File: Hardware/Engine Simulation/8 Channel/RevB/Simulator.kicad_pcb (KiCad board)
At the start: 2 copper layers, 100 x 80 mm, 69 parts, among them IC1 EL357NB_TA_-G, IC2 EL357NB_TA_-G, J1 Conn_02x20_Counter_Clockwise, J2 Conn_01x08, J3 Conn_01x08, J4 Conn_01x04, J5 Conn_01x04, J6 Conn_01x04, J7 Conn_01x10, J8 Conn_01x03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

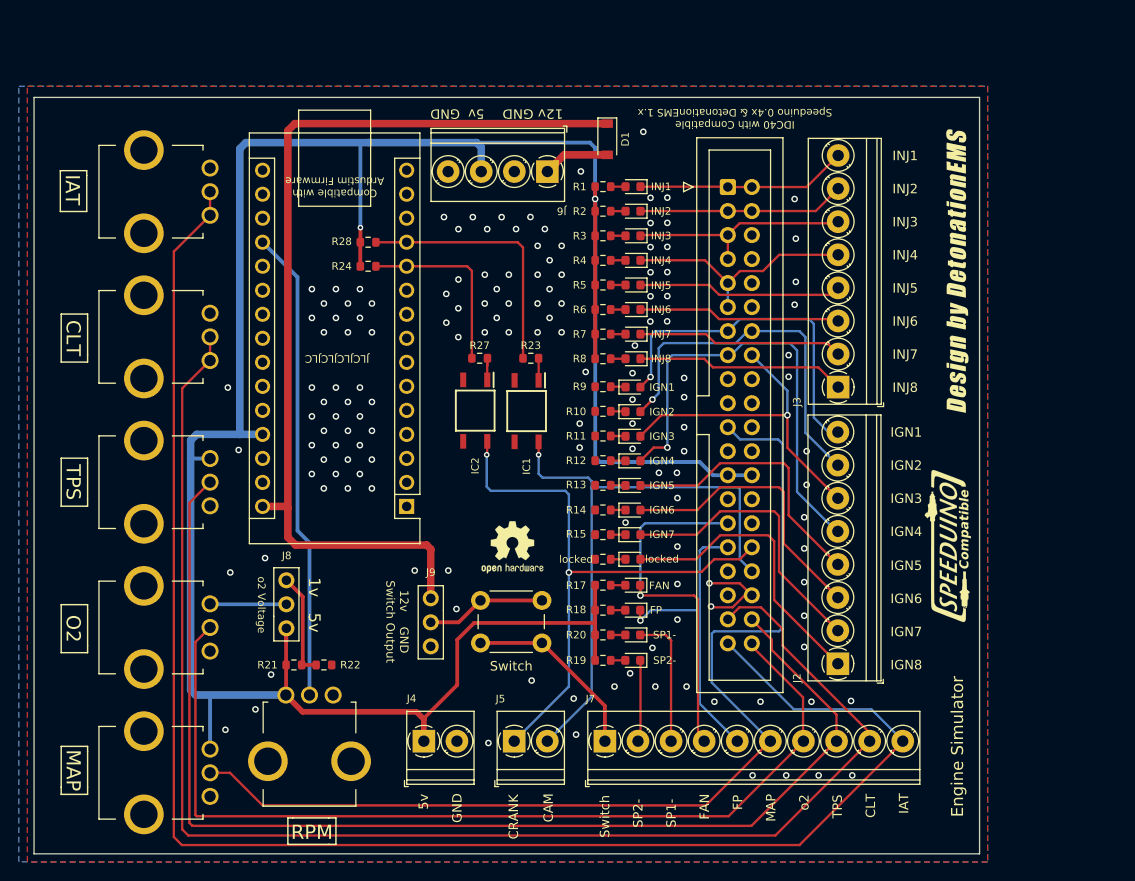
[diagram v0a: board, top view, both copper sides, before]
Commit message: Engine Simulator Upload Revision Correcton
Minor changes were made to RevB and uploaded as RevC by mistake. RevB minor layout changes for ease of use. Protection Zener added. Label correction.
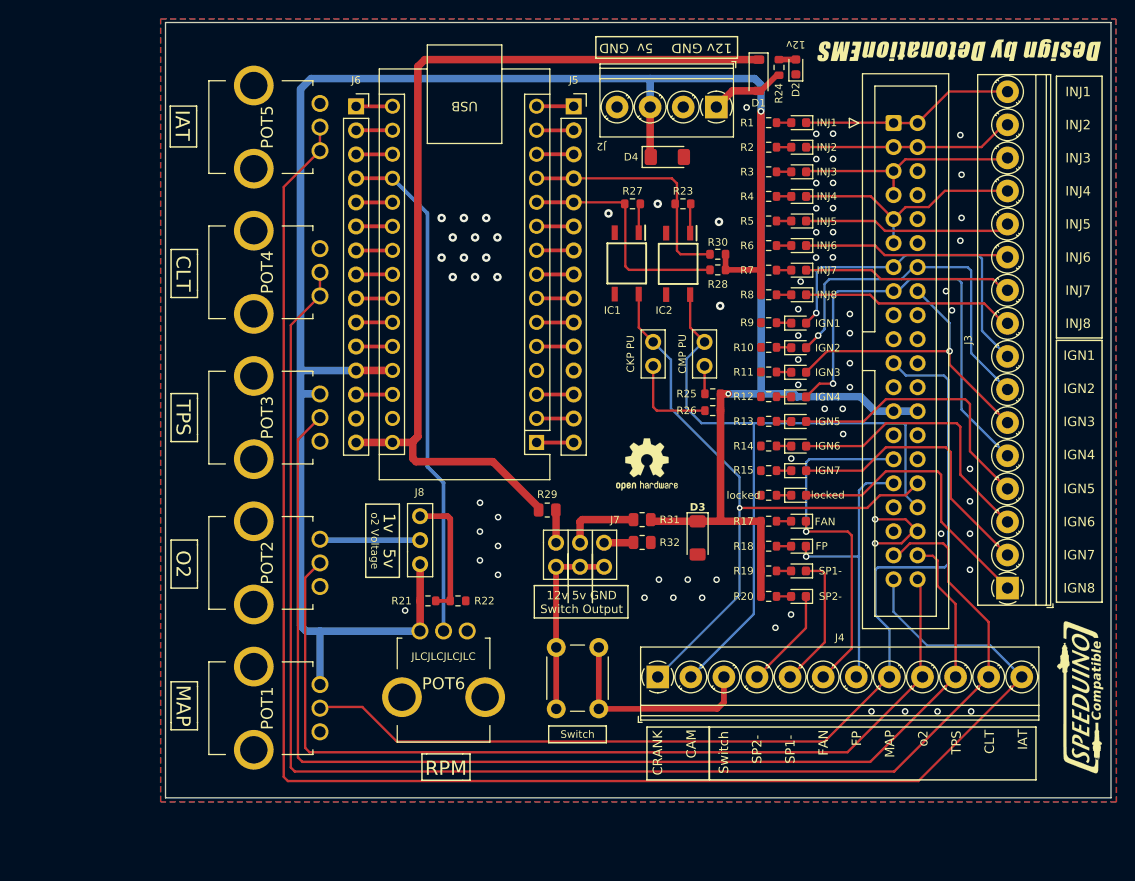
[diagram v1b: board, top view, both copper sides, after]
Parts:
- removed the J3 at (170.0, 96.5)
- removed the J4 at (126.1, 133.9)
- added D2: 12v, LED_SMD:LED_0603_1608Metric, F.Cu at (165.5, 62.6)
- added D3: ZMM5V6, Diode_SMD:D_MiniMELF, F.Cu at (155.1, 112.4)
- added D4: ZMM5V6, Diode_SMD:D_MiniMELF, F.Cu at (151.9, 72.1)
- added J10: CMP PU, Detonation:1x02-Proto, F.Cu at (155.8, 94.2)
- added J6: Conn_01x04, Connector_PinSocket_2.54mm:PinSocket_1x15_P2.54mm_Vertical, F.Cu at (119.0, 66.8)
- added J9: CKP PU, Detonation:1x02-Proto, F.Cu at (150.4, 94.2)
- added R25: 1k, Resistor_SMD:R_0603_1608Metric, F.Cu at (156.7, 97.2)
- added R26: 1k, Resistor_SMD:R_0603_1608Metric, F.Cu at (156.7, 99.0)
- added R29: 0r, Resistor_SMD:R_0805_2012Metric, F.Cu at (139.2, 109.5)
- added R30: 1k, Resistor_SMD:R_0603_1608Metric, F.Cu at (157.2, 82.4)
- added R31: 0r, Resistor_SMD:R_0805_2012Metric, F.Cu at (149.2, 110.5)
- added R32: 0r, Resistor_SMD:R_0805_2012Metric, F.Cu at (149.2, 112.9)
- D1: value SS34 -> B5819W
- J3: renamed from J2; footprint TerminalBlock_Phoenix:TerminalBlock_Phoenix_PT-1,5-8-3.5-H_1x08_P3.50mm_Horizontal -> TerminalBlock_Phoenix:TerminalBlock_Phoenix_PT-1,5-16-3.5-H_1x16_P3.50mm_Horizontal
- J4: renamed from J7; footprint TerminalBlock_Phoenix:TerminalBlock_Phoenix_PT-1,5-10-3.5-H_1x10_P3.50mm_Horizontal -> TerminalBlock_Phoenix:TerminalBlock_Phoenix_PT-1,5-12-3.5-H_1x12_P3.50mm_Horizontal
- J5: footprint TerminalBlock_Phoenix:TerminalBlock_Phoenix_PT-1,5-2-3.5-H_1x02_P3.50mm_Horizontal -> Connector_PinSocket_2.54mm:PinSocket_1x15_P2.54mm_Vertical
- J7: renamed from J9; footprint Detonation:3-PinSwitch -> Detonation:PinSocket 2x03
- POT1, POT2, POT3, POT4, POT5, POT6: footprint MyLibs:RV09AF4020KB10K -> Misc:RV09AF4020KB10K
- R1, R10, R11, R12, R13, R14, R15, R17, R18, R2, R3, R4, R5, R6, R7, R8, R9, locked: value 470 -> 1k
- R19: renamed from R20; value 470 -> 1k
- R20: renamed from R19; value 470 -> 1k
- R21, R23, R27: value 470 -> 470r
- R22: value 100 -> 100r
- R24, R28: value 10k -> 1k
- moved J5 67.4 mm to (142.0, 66.8)
- moved R24 48.3 mm to (163.7, 62.7), turned to 90 degrees
- moved R28 37.1 mm to (157.2, 84.1)
- moved G1 23.4 mm to (182.8, 60.8), turned to 180 degrees
- moved R27 23.0 mm to (148.2, 77.1)
- moved R23 22.9 mm to (153.5, 77.1)
- moved IC2 22.3 mm to (153.0, 83.4)
- moved IC1 22.3 mm to (147.6, 83.4)
- moved G2 21.3 mm to (195.5, 129.3)
- moved J3 19.6 mm to (187.9, 117.7)
- moved J2 19.1 mm to (157.1, 66.9)
- moved J1 18.8 mm to (175.8, 68.5)
- moved LED10 18.8 mm to (165.8, 92.3)
- moved LED14 18.8 mm to (165.8, 102.7)
- moved LED15 18.8 mm to (165.8, 105.3)
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- renumbered IC2 to IC1, IC1 to IC2, J6 to J2, LED20 to LED19, LED19 to LED20
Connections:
- A1 pad 1: unconnected-(A1-Pad1) -> MC-D1
- A1 pad 10: unconnected-(A1-Pad10) -> MC-D7
- A1 pad 13: unconnected-(A1-Pad13) -> MC-D10
- A1 pad 14: unconnected-(A1-Pad14) -> MC-D11
- A1 pad 15: unconnected-(A1-Pad15) -> MC-D12
- A1 pad 16: unconnected-(A1-Pad16) -> MC-D13
- A1 pad 17: unconnected-(A1-Pad17) -> +3.3V
- A1 pad 18: unconnected-(A1-Pad18) -> MC-AREF
- A1 pad 20: unconnected-(A1-Pad20) -> MC-A1
- A1 pad 21: unconnected-(A1-Pad21) -> MC-A2
- A1 pad 22: unconnected-(A1-Pad22) -> MC-A3
- A1 pad 23: unconnected-(A1-Pad23) -> MC-A4
- A1 pad 24: unconnected-(A1-Pad24) -> MC-A5
- A1 pad 25: unconnected-(A1-Pad25) -> MC-A6
- A1 pad 26: unconnected-(A1-Pad26) -> MC-A7
- A1 pad 28: unconnected-(A1-Pad28) -> MC-RESET-28
- A1 pad 3: unconnected-(A1-Pad3) -> MC-RESET-3
- A1 pad 5: unconnected-(A1-Pad5) -> MC-D2
- A1 pad 6: unconnected-(A1-Pad6) -> MC-D3
- A1 pad 7: unconnected-(A1-Pad7) -> MC-D4
- A1 pad 8: unconnected-(A1-Pad8) -> MC-D5
- A1 pad 9: unconnected-(A1-Pad9) -> MC-D6
- D1 pad 2: +BATT -> 12v-Unprotected
- J2 pad 1: +BATT -> 12v-Unprotected
- J4 pad 1: SWITCH -> CRANK-OUT
- J4 pad 10: IAT -> TPS
- J4 pad 2: SP2- -> CAM-OUT
- J4 pad 3: SP1- -> SWITCH
- J4 pad 4: FAN -> SP2-
- J4 pad 5: FP -> SP1-
- J4 pad 6: MAP -> FAN
- J4 pad 7: o2 -> FP
- J4 pad 8: TPS -> MAP
- J4 pad 9: CLT -> o2
- J5 pad 1: CRANK-OUT -> MC-D12
- J5 pad 2: CAM-OUT -> MC-D11
- J7 pad 1: +12V -> Net-(J7-Pin_1)
- J7 pad 2: SWITCH-Select -> Net-(J7-Pin_2)
- J7 pad 3: GND -> Net-(J7-Pin_3)
- R24 pad 1: +5V -> 12v-Unprotected
- R24 pad 2: CRANK -> Net-(D2-A)
- R28 pad 1: +5V -> CRANK
- R28 pad 2: CAM -> +5V
- SW1 pad 2: SWITCH-Select -> Net-(J7-Pin_2)
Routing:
- net Net-(J7-Pin_2): track 0.00 -> 20.1 mm
- net SWITCH-Select: track 12.7 -> 0.00 mm
- net CAM-OUT: track 63.9 -> 76.1 mm, vias 1 -> 0
- net Net-(J9-Pin_1): track 0.00 -> 9.98 mm
- net Net-(J7-Pin_3): track 0.00 -> 7.97 mm
- net 12v-Unprotected: track 0.00 -> 7.51 mm
- net +BATT: track 7.06 -> 0.00 mm
- net CRANK-OUT: track 62.9 -> 68.4 mm, vias 2 -> 1
- net CRANK: track 19.9 -> 24.8 mm
- net MC-A0: track 49.9 -> 54.0 mm
- net MC-D6: track 0.00 -> 3.91 mm
- net MC-D4: track 0.00 -> 3.91 mm
- net MC-D12: track 0.00 -> 3.91 mm
- net MC-D10: track 0.00 -> 3.91 mm
- net MC-RESET-3: track 0.00 -> 3.91 mm
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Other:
- board size 100 x 80 mm -> 100 x 82 mm
- board text added: "12v 5v GND Switch Output"
- board text added: "DetoSim8 - RevB"
- board text added: "locked"
- board text removed: "12v GND Switch Output"
- board text removed: "5v"
- board text removed: "Compatible with Ardustim Firmware"
- board text removed: "DetonationEMS © 2022 Aaron S."
- board text removed: "Engine Simulator"
- board text removed: "GND"
- board text removed: "IDC40 with Compatible Speeduino 0.4x & DetonationEMS 1.x"
- board text removed: "Sim8-B"
